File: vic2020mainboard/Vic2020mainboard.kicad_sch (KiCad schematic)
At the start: 13 parts

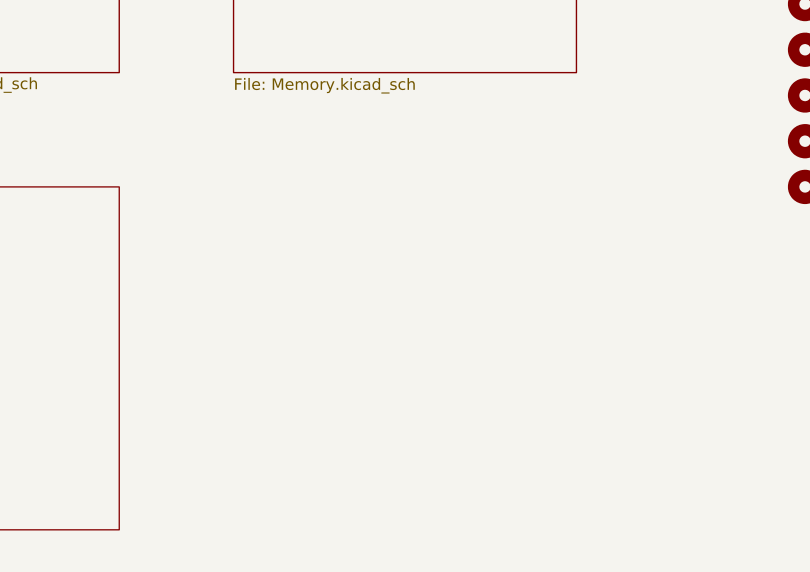
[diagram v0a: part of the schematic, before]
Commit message: Added power supply circuit for 9V AC input
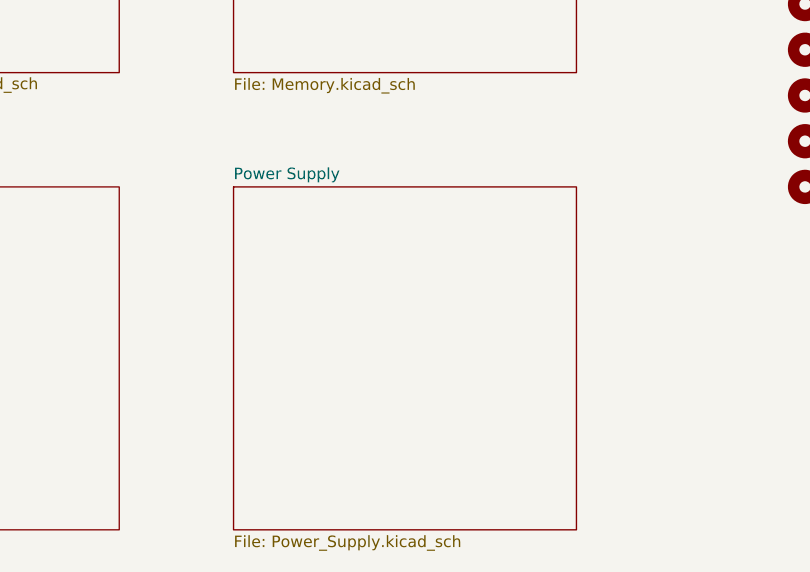
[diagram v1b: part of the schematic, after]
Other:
- added sheet Power Supply (Power_Supply.kicad_sch)
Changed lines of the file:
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@@
+	)
+	(sheet
+		(at 127 88.9)
+		(size 38.1 38.1)
+		(exclude_from_sim no)
+		(in_bom yes)
+		(on_board yes)
+		(dnp no)
+		(fields_autoplaced yes)
+		(stroke
+			(width 0.1524)
+			(type solid)
+		)
+		(fill
+			(color 0 0 0 0)
+		)
+		(property "Sheetname" "Power Supply"
+			(at 127 88.1884 0)
+			(show_name no)
+			(do_not_autoplace no)
+			(effects
+				(font
+					(size 1.27 1.27)
+				)
+				(justify left bottom)
+			)
+		)
+		(property "Sheetfile" "Power_Supply.kicad_sch"
+			(at 127 127.5846 0)
+			(show_name no)
+			(do_not_autoplace no)
+			(effects
+				(font
+					(size 1.27 1.27)
+				)
+				(justify left top)
+			)
+		)
+		(instances
+			(project "Vic2020mainboard"
+				(path "/f98df84e-f5f2-4c35-84be-6093352134d0"
+					(page "6")
+				)
+			)
+		)
 	)
 	(sheet
